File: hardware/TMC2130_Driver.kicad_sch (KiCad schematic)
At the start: 35 parts, among them J1 PCIe_Stepper, J2 Conn_01x04_Male, J3 Screw_Terminal_01x02, U1 TMC2130, U2 24LC02

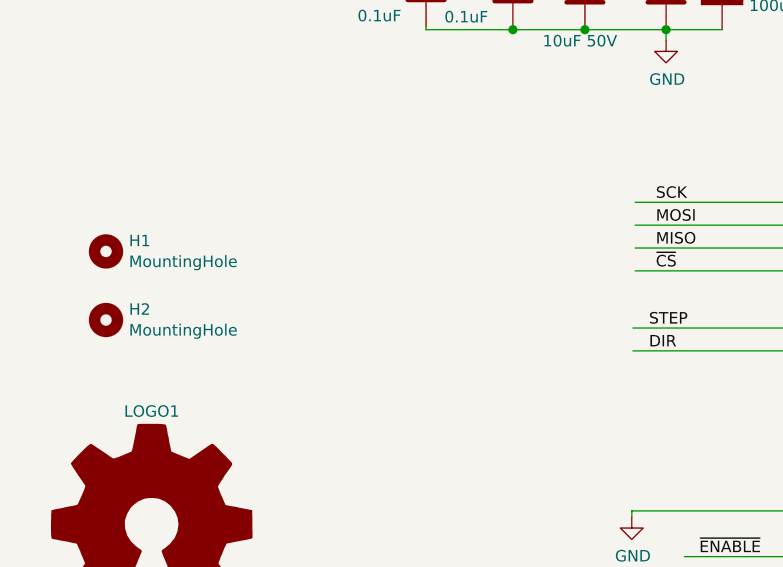
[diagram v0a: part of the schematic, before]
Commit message: Update of PCBs
- added tooling holes
- added order number location under components

Updated projects:
- DRV-Stepstick
- TMC2209
- TMC2130
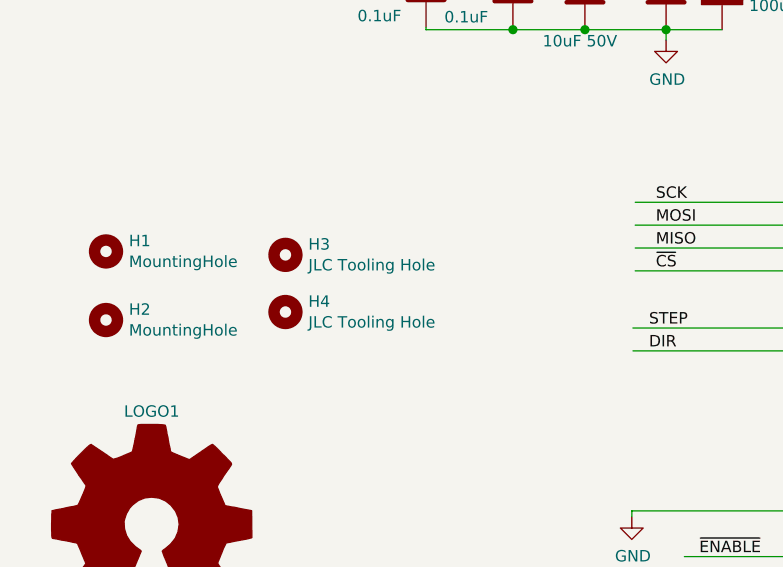
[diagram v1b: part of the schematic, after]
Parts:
- added H3, H4: JLC Tooling Hole, PrntrBoardV2:JLC_Tool_hole, symbol Mechanical:MountingHole
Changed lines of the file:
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@@
 (kicad_sch (version 20201015) (generator eeschema)
-  (page 1 1)
   (paper "A4")
   (junction (at 80.137 28.194) (diameter 1.016) (color 0 0 0 0))
@@
   (junction (at 254 91.44) (diameter 1.016) (color 0 0 0 0))
   (junction (at 254 93.98) (diameter 1.016) (color 0 0 0 0))
-  (no_connect (at 111.252 94.234))
+  (no_connect (at 111.252 82.804))
+  (no_connect (at 111.252 85.344))
   (no_connect (at 111.252 87.884))
   (no_connect (at 111.252 91.694))
+  (no_connect (at 111.252 94.234))
   (no_connect (at 164.592 65.024))
-  (no_connect (at 111.252 85.344))
-  (no_connect (at 111.252 82.804))
   (wire (pts (xy 70.485 28.194) (xy 80.137 28.194))
     (stroke (width 0) (type solid) (color 0 0 0 0))
@@
     )
     (property "Datasheet" "~" (id 3) (at 34.925 75.565 0)
+      (effects (font (size 1.27 1.27)) hide)
+    )
+  )
+  (symbol (lib_id "Mechanical:MountingHole") (at 54.864 68.326 0) (unit 1)
+    (in_bom no) (on_board yes)
+    (property "Reference" "H3" (id 0) (at 57.404 67.1576 0)
+      (effects (font (size 1.27 1.27)) (justify left))
+    )
+    (property "Value" "JLC Tooling Hole" (id 1) (at 57.404 69.469 0)
+      (effects (font (size 1.27 1.27)) (justify left))
+    )
+    (property "Footprint" "PrntrBoardV2:JLC_Tool_hole" (id 2) (at 54.864 68.326 0)
+      (effects (font (size 1.27 1.27)) hide)
+    )
+    (property "Datasheet" "~" (id 3) (at 54.864 68.326 0)
+      (effects (font (size 1.27 1.27)) hide)
+    )
+  )
+  (symbol (lib_id "Mechanical:MountingHole") (at 54.864 74.676 0) (unit 1)
+    (in_bom no) (on_board yes)
+    (property "Reference" "H4" (id 0) (at 57.404 73.5076 0)
+      (effects (font (size 1.27 1.27)) (justify left))
+    )
+    (property "Value" "JLC Tooling Hole" (id 1) (at 57.404 75.819 0)
+      (effects (font (size 1.27 1.27)) (justify left))
+    )
+    (property "Footprint" "PrntrBoardV2:JLC_Tool_hole" (id 2) (at 54.864 74.676 0)
+      (effects (font (size 1.27 1.27)) hide)
+    )
+    (property "Datasheet" "~" (id 3) (at 54.864 74.676 0)
       (effects (font (size 1.27 1.27)) hide)
     )
@@
       (reference "H2") (unit 1) (value "MountingHole") (footprint "MountingHole:MountingHole_2.7mm_M2.5")
     )
+    (path "/6b360de5-1019-4f01-848a-8d87a890d865"
+      (reference "H3") (unit 1) (value "JLC Tooling Hole") (footprint "PrntrBoardV2:JLC_Tool_hole")
+    )
+    (path "/3ae614fa-e4c5-4abd-849b-670f72506669"
+      (reference "H4") (unit 1) (value "JLC Tooling Hole") (footprint "PrntrBoardV2:JLC_Tool_hole")
+    )
     (path "/00000000-0000-0000-0000-00005d9a9126"
